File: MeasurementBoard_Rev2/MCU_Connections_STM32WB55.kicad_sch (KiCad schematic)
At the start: 2 parts, among them J1 Conn_02x19_Odd_Even, J2 Conn_02x19_Odd_Even

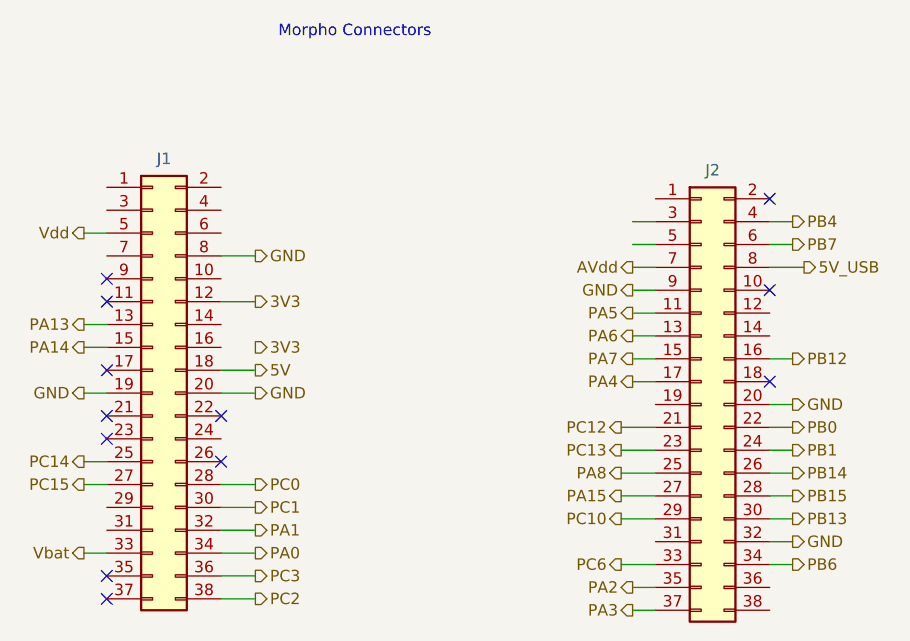
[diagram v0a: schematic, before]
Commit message: Finished Measurement Board Update Minus Heater Board Connections
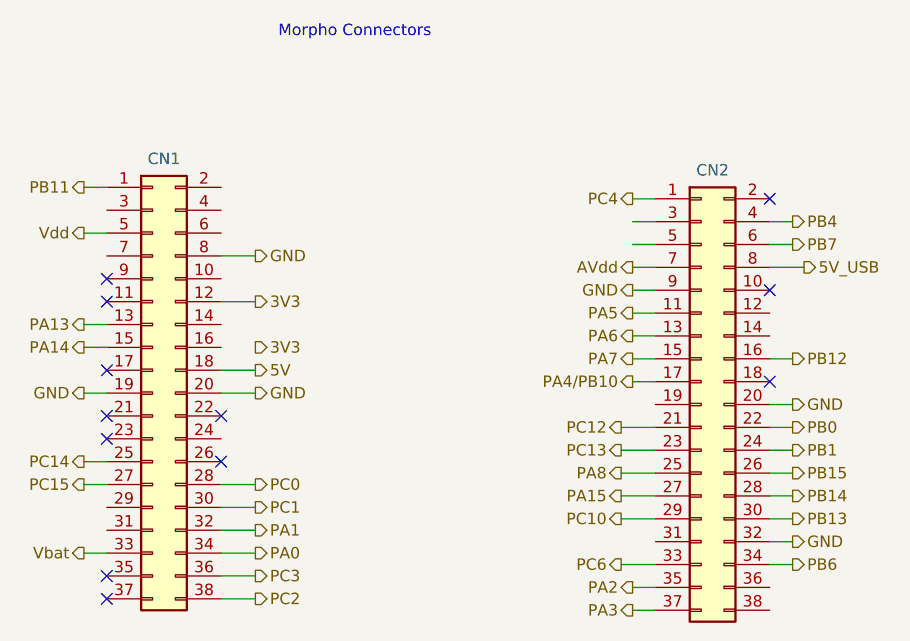
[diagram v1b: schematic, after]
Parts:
- renumbered J1 to CN1, J2 to CN2
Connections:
- net PB14: now also CN2.28 (Pin_28); no longer CN2.26 (Pin_26)
- net PB15: now also CN2.26 (Pin_26); no longer CN2.28 (Pin_28)
- net PB11: now reaches CN1.1 (Pin_1)
- net PC4: now reaches CN2.1 (Pin_1)
- net PA4 renamed PA4/PB10

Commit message: Nearly Finalized Boards
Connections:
- net PB2: now reaches CN1.2 (Pin_2)
- net PE4: now reaches CN1.4 (Pin_4)
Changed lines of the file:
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@@
+	(wire
+		(pts
+			(xy 57.15 45.72) (xy 59.69 45.72)
+		)
+		(stroke
+			(width 0)
+			(type default)
+		)
+	)
 	(wire
 		(pts
@@
 		(pts
 			(xy 105.41 64.77) (xy 102.87 64.77)
+		)
+		(stroke
+			(width 0)
+			(type default)
+		)
+	)
+	(wire
+		(pts
+			(xy 57.15 43.18) (xy 59.69 43.18)
 		)
 		(stroke
@@
 		)
 	)
+	(hierarchical_label "PE4"
+		(shape output)
+		(at 59.69 45.72 0)
+		(fields_autoplaced yes)
+		(effects
+			(font
+				(size 1.27 1.27)
+			)
+			(justify left)
+		)
+	)
 	(hierarchical_label "Vdd"
 		(shape output)
@@
 		)
 	)
+	(hierarchical_label "PB2"
+		(shape output)
+		(at 59.69 43.18 0)
+		(fields_autoplaced yes)
+		(effects
+			(font
+				(size 1.27 1.27)
+			)
+			(justify left)
+		)
+	)

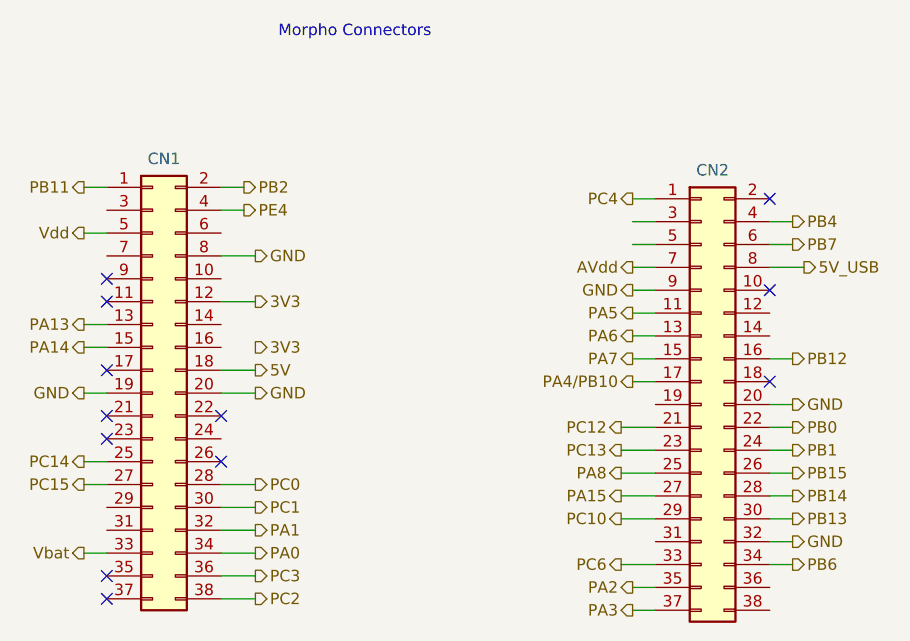
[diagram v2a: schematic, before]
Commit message: Finished Measurement Board Fixes Schematic and PCB
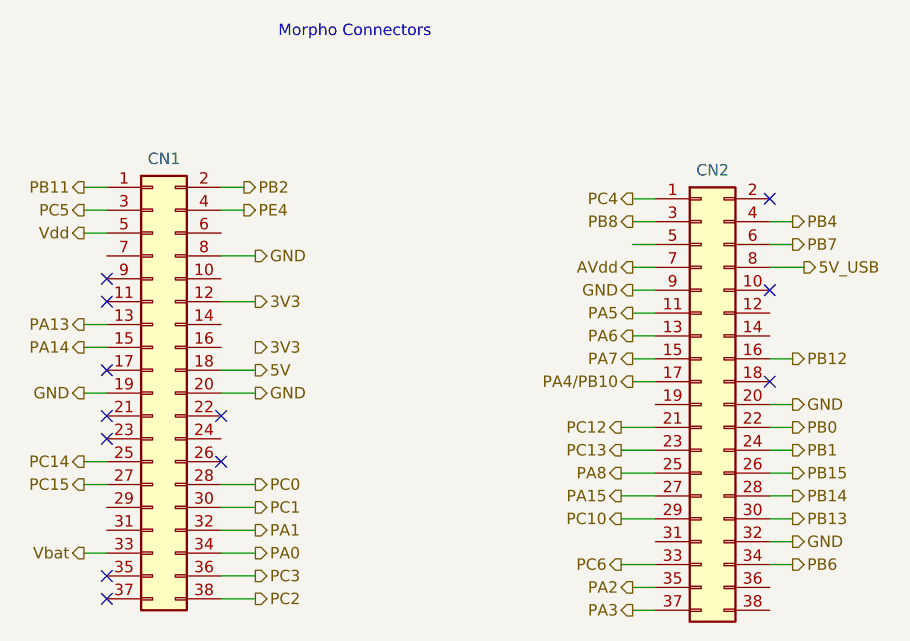
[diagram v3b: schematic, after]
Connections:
- net PC5: now reaches CN1.3 (Pin_3)
- net PB8: now reaches CN2.3 (Pin_3)
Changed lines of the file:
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@@
+	(wire
+		(pts
+			(xy 41.91 45.72) (xy 44.45 45.72)
+		)
+		(stroke
+			(width 0)
+			(type default)
+		)
+	)
 	(wire
 		(pts
@@
 		)
 	)
+	(hierarchical_label "PC5"
+		(shape output)
+		(at 41.91 45.72 180)
+		(fields_autoplaced yes)
+		(effects
+			(font
+				(size 1.27 1.27)
+			)
+			(justify right)
+		)
+	)
 	(hierarchical_label "PC12"
 		(shape output)
@@
 		)
 	)
+	(hierarchical_label "PB8"
+		(shape output)
+		(at 102.87 46.99 180)
+		(fields_autoplaced yes)
+		(effects
+			(font
+				(size 1.27 1.27)
+			)
+			(justify right)
+		)
+	)
